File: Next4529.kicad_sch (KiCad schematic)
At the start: 13 parts, among them U1 74LVC1G3157, U2 74LVC1G3157, U3 74LVC1G3157, U4 74LVC1G3157, U5 74LVC1G3157, U6 74LVC1G3157, U7 74LVC1G3157, U8 SLG46824V, U9 14529

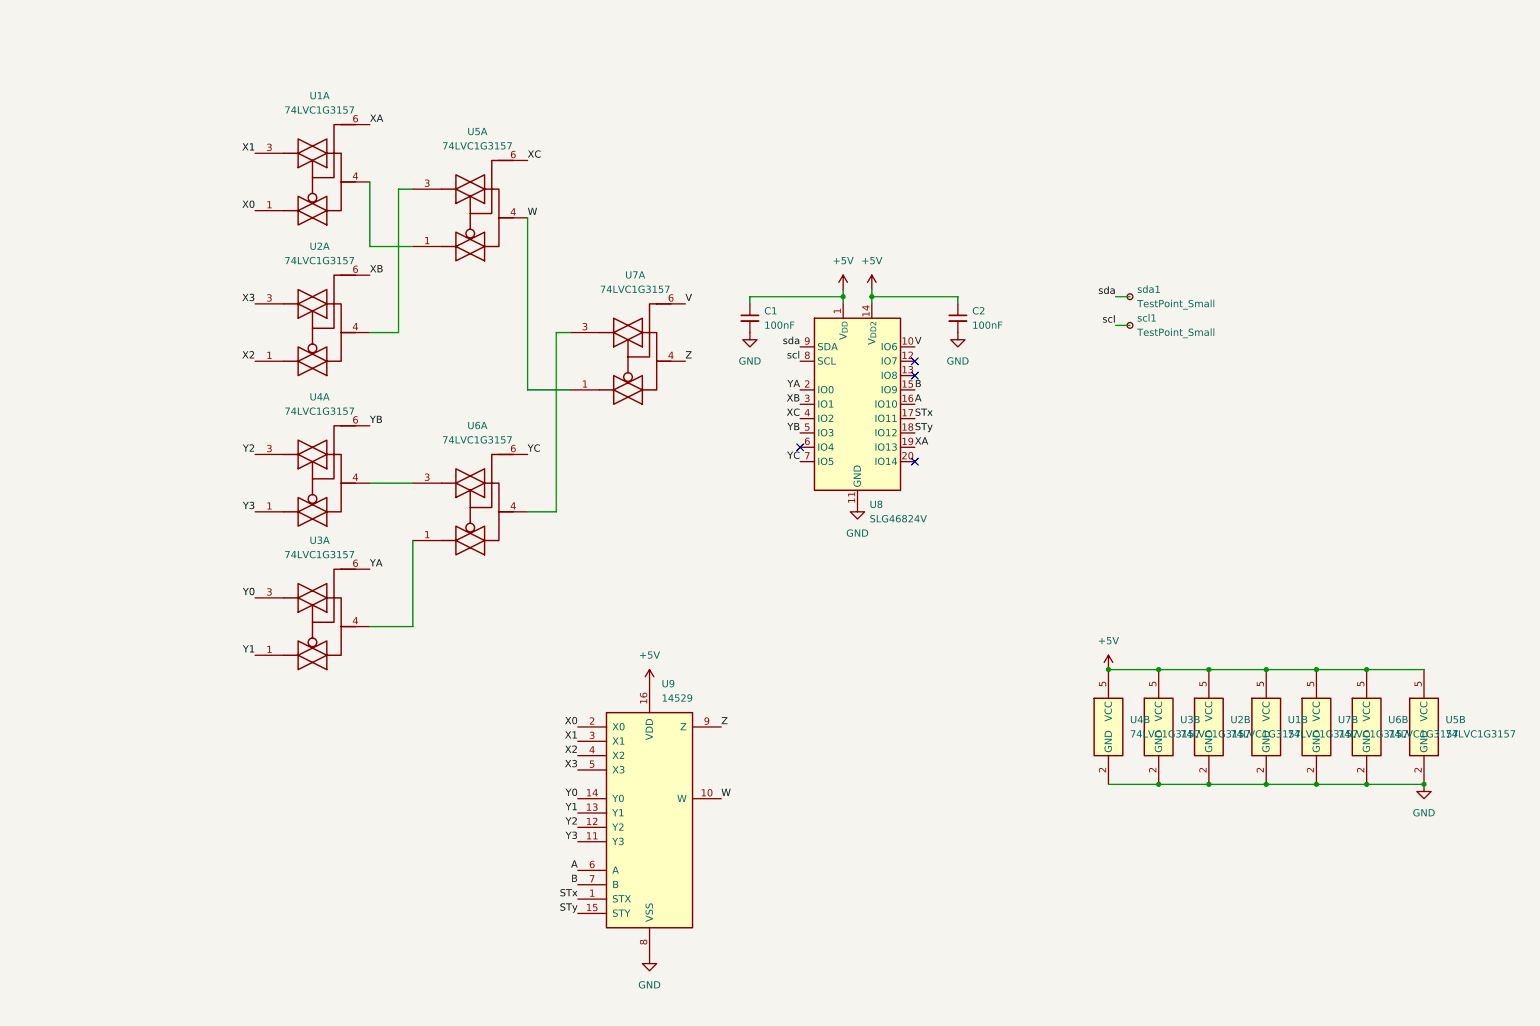
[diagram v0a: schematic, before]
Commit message: add notes to schematic
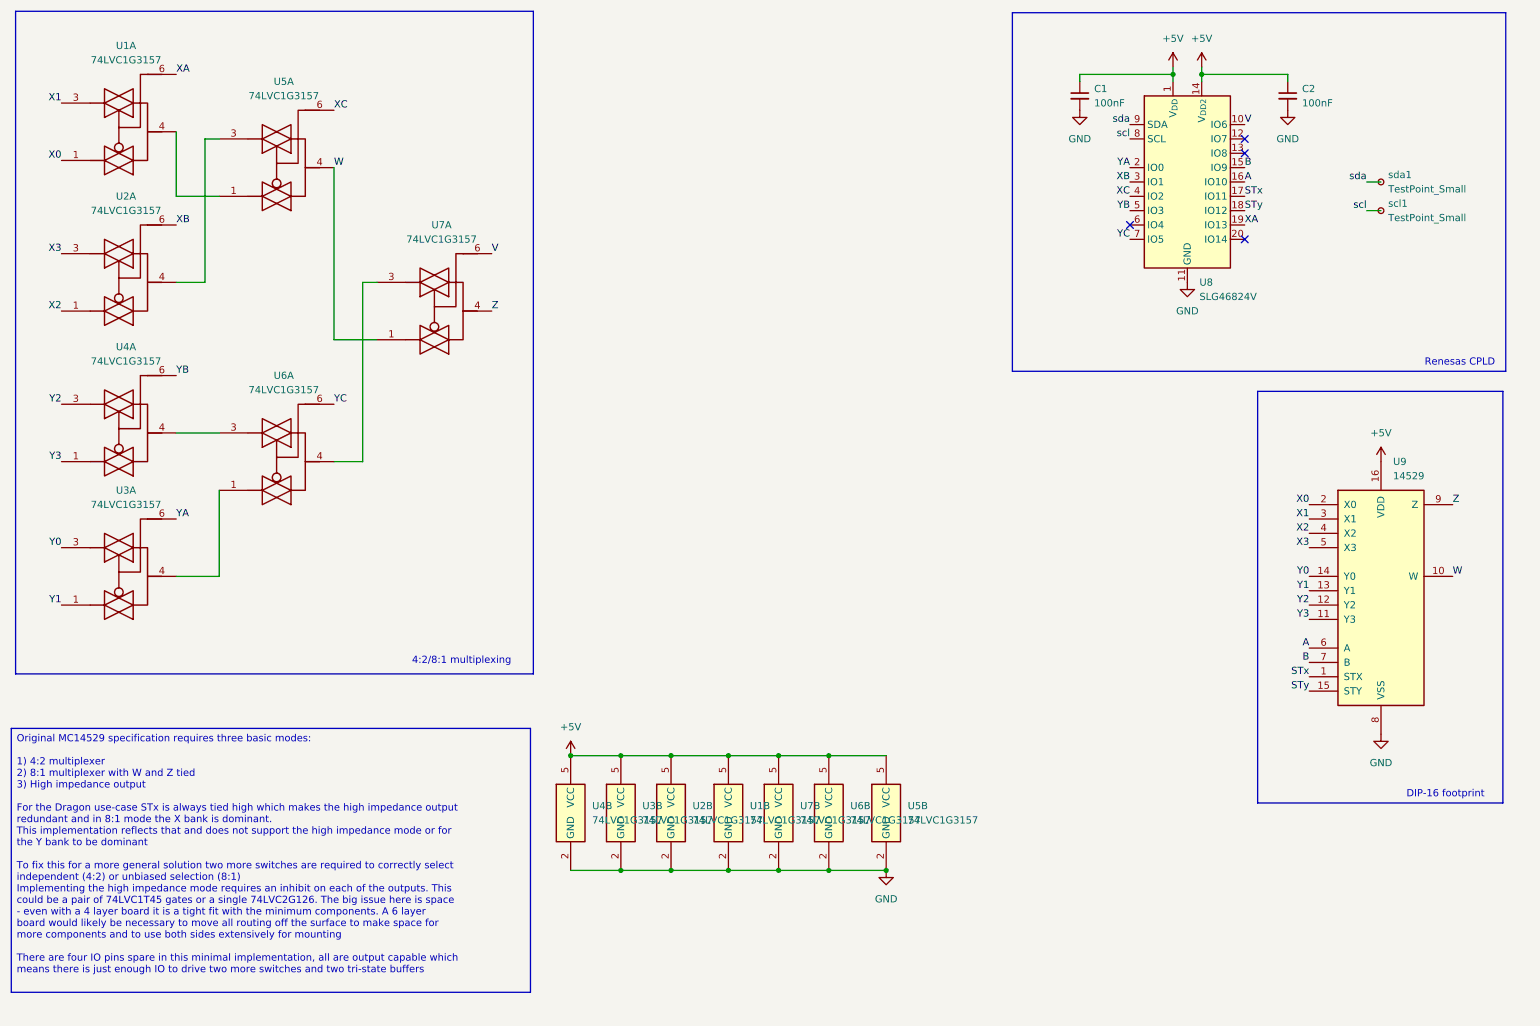
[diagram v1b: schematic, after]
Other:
- note added: "4:2/8:1 multiplexing"
- note added: "DIP-16 footprint"
- note added: "Renesas CPLD"
- moved on the sheet: C1, C2, U1A, U1B, U2A, U2B, U3A, U3B, U4A, U4B, U5A, U5B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

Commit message: redesign
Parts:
- added U10, U9: 74LVC1G66DSF, Package_SON:Texas_USON-6_1x1.45mm_P0.5mm_SMD, symbol 74xGxx:74LVC1G66
- added U8: 74LVC1G3157, Package_SON:Texas_USON-6_1x1.45mm_P0.5mm_SMD, symbol 74xGxx:74LVC1G3157
- U1, U2, U3, U4, U5, U6, U7: footprint Package_TO_SOT_SMD:Vishay_PowerPAK_SC70-6L_Dual -> Package_SON:Texas_USON-6_1x1.45mm_P0.5mm_SMD
- renumbered U9 to IC1, U8 to U11
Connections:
- net +5V: now also U10.5 (VCC), U8.5 (VCC), U9.5 (VCC)
- net GND: now also U10.3 (GND), U8.2 (GND), U9.3 (GND)
- net W: now also U10.2; no longer U5.4, U7.1
- net YA: now also U11.7 (IO5); no longer U11.2 (IO0)
- net YC: now also U11.2 (IO0); no longer U11.7 (IO5)
- net Z: now also U9.2; no longer U7.4
- net Y01: now reaches U3.4, U6.1
- net X01: now reaches U5.3
- net X01: now also U1.4; no longer U2.4
- net X23: now reaches U5.1
- net X23: now also U2.4; no longer U1.4
- net WC: now reaches U11.12 (IO7)
- net WC: now also U8.6
- net OE: now reaches U11.13 (IO8)
- net OE: now also U10.4, U9.4
- net Y23: now reaches U4.4, U6.3
- net Y: now reaches U6.4, U7.3
- net Y: now also U8.1
- net V renamed ZC
- new net WG: U10.1, U8.4
- new net X: U5.4, U7.1, U8.3
- new net ZG: U7.4, U9.1
- no-connect marks 4 -> 2
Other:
- moved on the sheet: U1B, U2B, U3B, U4B, U5A, U5B, U6B, U7A, U7B
